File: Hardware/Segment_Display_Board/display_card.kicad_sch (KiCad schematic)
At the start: 4 parts, among them J501 Bottom Conn, J502 Top Conn, U501 SN74HC595

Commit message: Fix stuff i guess goodnight"
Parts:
- added JP501, JP502: SolderJumper_2_Bridged, Jumper:SolderJumper-2_P1.3mm_Bridged_Pad1.0x1.5mm, symbol Jumper:SolderJumper_2_Bridged
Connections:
- net CLOCK_IN: now also JP502.1 (A)
- net LATCH_IN: now also JP501.1 (A)
- new net CLOCK_OUT: JP502.2 (B)
- new net LATCH_OUT: JP501.2 (B)
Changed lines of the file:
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@@
     (title "Days Without Incident Sign")
     (date "2022-06-24")
-    (rev "v0.1-RC1")
+    (rev "${REVISION}")
     (company "FRC 1721")
+    (comment 4 "Release: ${FULL_REVISION}")
   )
   (no_connect (at 25.4 116.205))
@@
     (stroke (width 0) (type default) (color 0 0 0 0))
   )
+  (wire (pts (xy 127.635 118.745) (xy 129.54 118.745))
+    (stroke (width 0) (type default) (color 0 0 0 0))
+  )
   (wire (pts (xy 119.38 93.345) (xy 111.76 93.345))
     (stroke (width 0) (type default) (color 0 0 0 0))
@@
     (stroke (width 0) (type default) (color 0 0 0 0))
   )
+  (wire (pts (xy 127.635 114.935) (xy 129.54 114.935))
+    (stroke (width 0) (type default) (color 0 0 0 0))
+  )
   (wire (pts (xy 24.13 92.075) (xy 24.13 79.375))
     (stroke (width 0) (type default) (color 0 0 0 0))
@@
     (stroke (width 0) (type default) (color 0 0 0 0))
   )
+  (wire (pts (xy 118.11 118.745) (xy 120.015 118.745))
+    (stroke (width 0) (type default) (color 0 0 0 0))
+  )
   (wire (pts (xy 129.54 111.125) (xy 111.76 111.125))
     (stroke (width 0) (type default) (color 0 0 0 0))
@@
     (stroke (width 0) (type default) (color 0 0 0 0))
   )
-  (wire (pts (xy 120.65 113.665) (xy 129.54 113.665))
+  (wire (pts (xy 118.11 114.935) (xy 120.015 114.935))
     (stroke (width 0) (type default) (color 0 0 0 0))
   )
@@
     (stroke (width 0) (type default) (color 0 0 0 0))
   )
-  (wire (pts (xy 120.65 116.205) (xy 129.54 116.205))
-    (stroke (width 0) (type default) (color 0 0 0 0))
-  )
   (wire (pts (xy 93.98 95.885) (xy 74.93 95.885))
     (stroke (width 0) (type default) (color 0 0 0 0))
@@
     (effects (font (size 1.27 1.27)) (justify right))
   )
-  (hierarchical_label "CLOCK_OUT" (shape output) (at 129.54 116.205 0)
+  (hierarchical_label "CLOCK_OUT" (shape output) (at 129.54 118.745 0)
     (effects (font (size 1.27 1.27)) (justify left))
   )
@@
     (effects (font (size 1.27 1.27)) (justify right))
   )
-  (hierarchical_label "LATCH_IN" (shape input) (at 120.65 113.665 180)
-    (effects (font (size 1.27 1.27)) (justify right))
-  )
-  (hierarchical_label "CLOCK_IN" (shape input) (at 120.65 116.205 180)
-    (effects (font (size 1.27 1.27)) (justify right))
-  )
-  (hierarchical_label "LATCH_OUT" (shape output) (at 129.54 113.665 0)
+  (hierarchical_label "LATCH_IN" (shape input) (at 118.11 114.935 180)
+    (effects (font (size 1.27 1.27)) (justify right))
+  )
+  (hierarchical_label "CLOCK_IN" (shape input) (at 118.11 118.745 180)
+    (effects (font (size 1.27 1.27)) (justify right))
+  )
+  (hierarchical_label "LATCH_OUT" (shape output) (at 129.54 114.935 0)
     (effects (font (size 1.27 1.27)) (justify left))
+  )
+  (symbol (lib_id "Jumper:SolderJumper_2_Bridged") (at 123.825 118.745 0) (unit 1)
+    (in_bom yes) (on_board yes)
+    (property "Reference" "JP502" (id 0) (at 123.825 121.92 0))
+    (property "Value" "SolderJumper_2_Bridged" (id 1) (at 123.825 115.57 0)
+      (effects (font (size 1.27 1.27)) hide)
+    )
+    (property "Footprint" "Jumper:SolderJumper-2_P1.3mm_Bridged_Pad1.0x1.5mm" (id 2) (at 123.825 118.745 0)
+      (effects (font (size 1.27 1.27)) hide)
+    )
+    (property "Datasheet" "~" (id 3) (at 123.825 118.745 0)
+      (effects (font (size 1.27 1.27)) hide)
+    )
+    (pin "1")
+    (pin "2")
   )
   (symbol (lib_id "Device:C_Small") (at 88.9 79.375 0) (unit 1)
@@
       (effects (font (size 1.27 1.27)) hide)
     )
+    (pin "1")
+    (pin "2")
+  )
+  (symbol (lib_id "Jumper:SolderJumper_2_Bridged") (at 123.825 114.935 0) (unit 1)
+    (in_bom yes) (on_board yes)
+    (property "Reference" "JP501" (id 0) (at 123.825 112.395 0))
+    (property "Value" "SolderJumper_2_Bridged" (id 1) (at 123.825 111.76 0)
+      (effects (font (size 1.27 1.27)) hide)
+    )
+    (property "Footprint" "Jumper:SolderJumper-2_P1.3mm_Bridged_Pad1.0x1.5mm" (id 2) (at 123.825 114.935 0)
+      (effects (font (size 1.27 1.27)) hide)
+    )
+    (property "Datasheet" "~" (id 3) (at 123.825 114.935 0)
+      (effects (font (size 1.27 1.27)) hide)
+    )

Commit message: include fixups fro EE
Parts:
- C501: value 10uF -> 100nF
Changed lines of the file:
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@@
-    (pin "2")
-  )
-  (symbol (lib_id "Device:C_Small") (at 88.9 79.375 0) (unit 1)
-    (in_bom yes) (on_board yes) (fields_autoplaced)
-    (property "Reference" "C501" (id 0) (at 91.44 78.1112 0)
-      (effects (font (size 1.27 1.27)) (justify left))
-    )
-    (property "Value" "10uF" (id 1) (at 91.44 80.6512 0)
-      (effects (font (size 1.27 1.27)) (justify left))
-    )
-    (property "Footprint" "Capacitor_SMD:C_0805_2012Metric" (id 2) (at 88.9 79.375 0)
-      (effects (font (size 1.27 1.27)) hide)
-    )
-    (property "Datasheet" "~" (id 3) (at 88.9 79.375 0)
-      (effects (font (size 1.27 1.27)) hide)
-    )
-    (pin "1")
     (pin "2")
   )
@@
     (pin "1")
   )
+  (symbol (lib_id "Device:C_Small") (at 88.9 79.375 0) (unit 1)
+    (in_bom yes) (on_board yes)
+    (property "Reference" "C501" (id 0) (at 91.44 79.375 0)
+      (effects (font (size 1.27 1.27)) (justify left))
+    )
+    (property "Value" "100nF" (id 1) (at 91.44 81.915 0)
+      (effects (font (size 1.27 1.27)) (justify left))
+    )
+    (property "Footprint" "Capacitor_SMD:C_0805_2012Metric" (id 2) (at 88.9 79.375 0)
+      (effects (font (size 1.27 1.27)) hide)
+    )
+    (property "Datasheet" "~" (id 3) (at 88.9 79.375 0)
+      (effects (font (size 1.27 1.27)) hide)
+    )
+    (pin "1")
+    (pin "2")
+  )
   (symbol (lib_id "power:GND") (at 34.29 82.55 0) (unit 1)

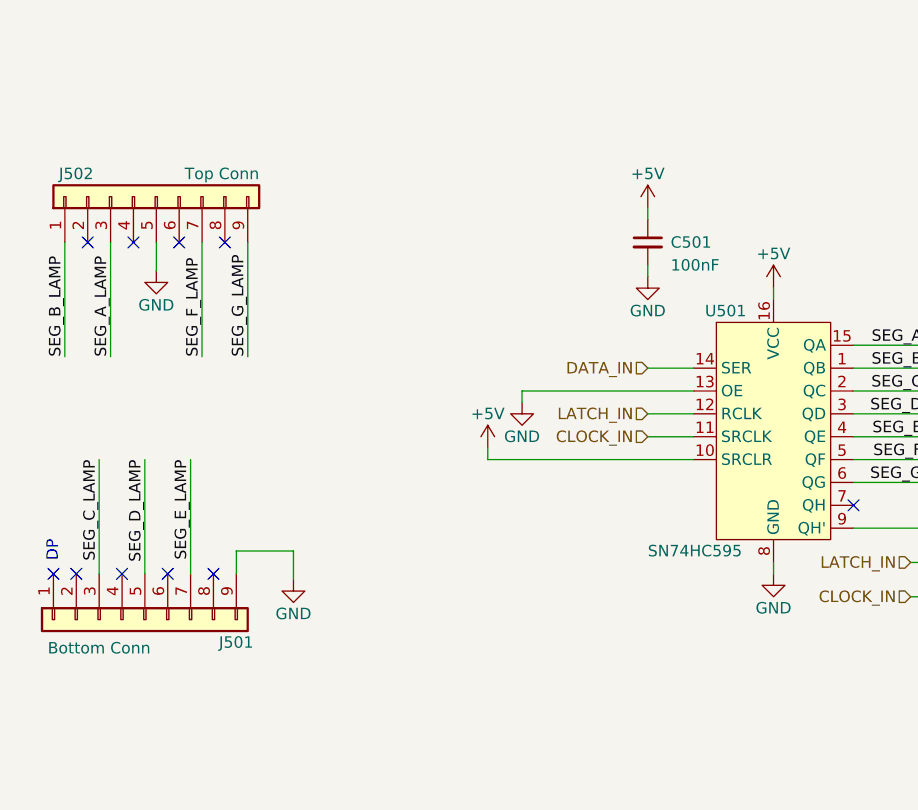
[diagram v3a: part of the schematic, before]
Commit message: Use new 5in symbol and footprint
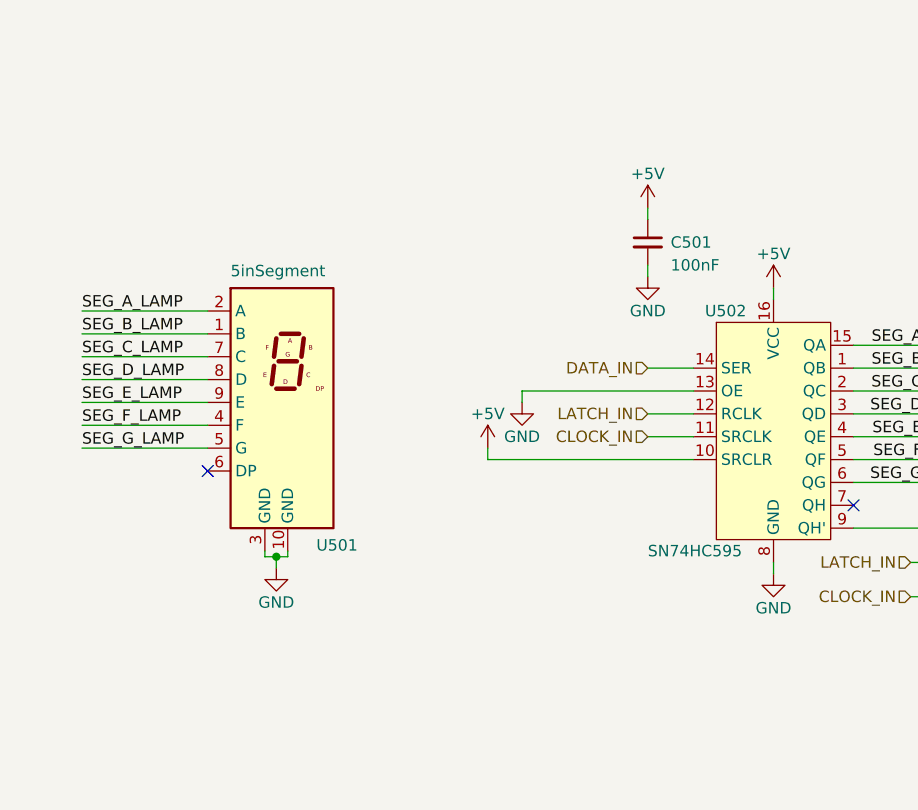
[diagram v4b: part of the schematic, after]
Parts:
- removed J501: Bottom Conn, Connector_PinSocket_2.54mm:PinSocket_1x09_P2.54mm_Vertical, symbol Connector_Generic:Conn_01x09
- removed J502: Top Conn, Connector_PinSocket_2.54mm:PinSocket_1x09_P2.54mm_Vertical, symbol Connector_Generic:Conn_01x09
- added U501: 5inSegment, KenwoodFox:5inSegment, symbol KenwoodFox:5inSegment
- renumbered U501 to U502
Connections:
- net GND: now also U501.10 (GND), U501.3 (GND)
- net SEG_A_LAMP: now also U501.2 (A)
- net SEG_B_LAMP: now also U501.1 (B)
- net SEG_C_LAMP: now also U501.7 (C)
- net SEG_D_LAMP: now also U501.8 (D)
- net SEG_E_LAMP: now also U501.9 (E)
- net SEG_F_LAMP: now also U501.4 (F)
- net SEG_G_LAMP: now also U501.5 (G)
- no-connect marks 10 -> 2
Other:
- note removed: "DP"
